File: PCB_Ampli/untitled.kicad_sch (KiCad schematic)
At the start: 58 parts

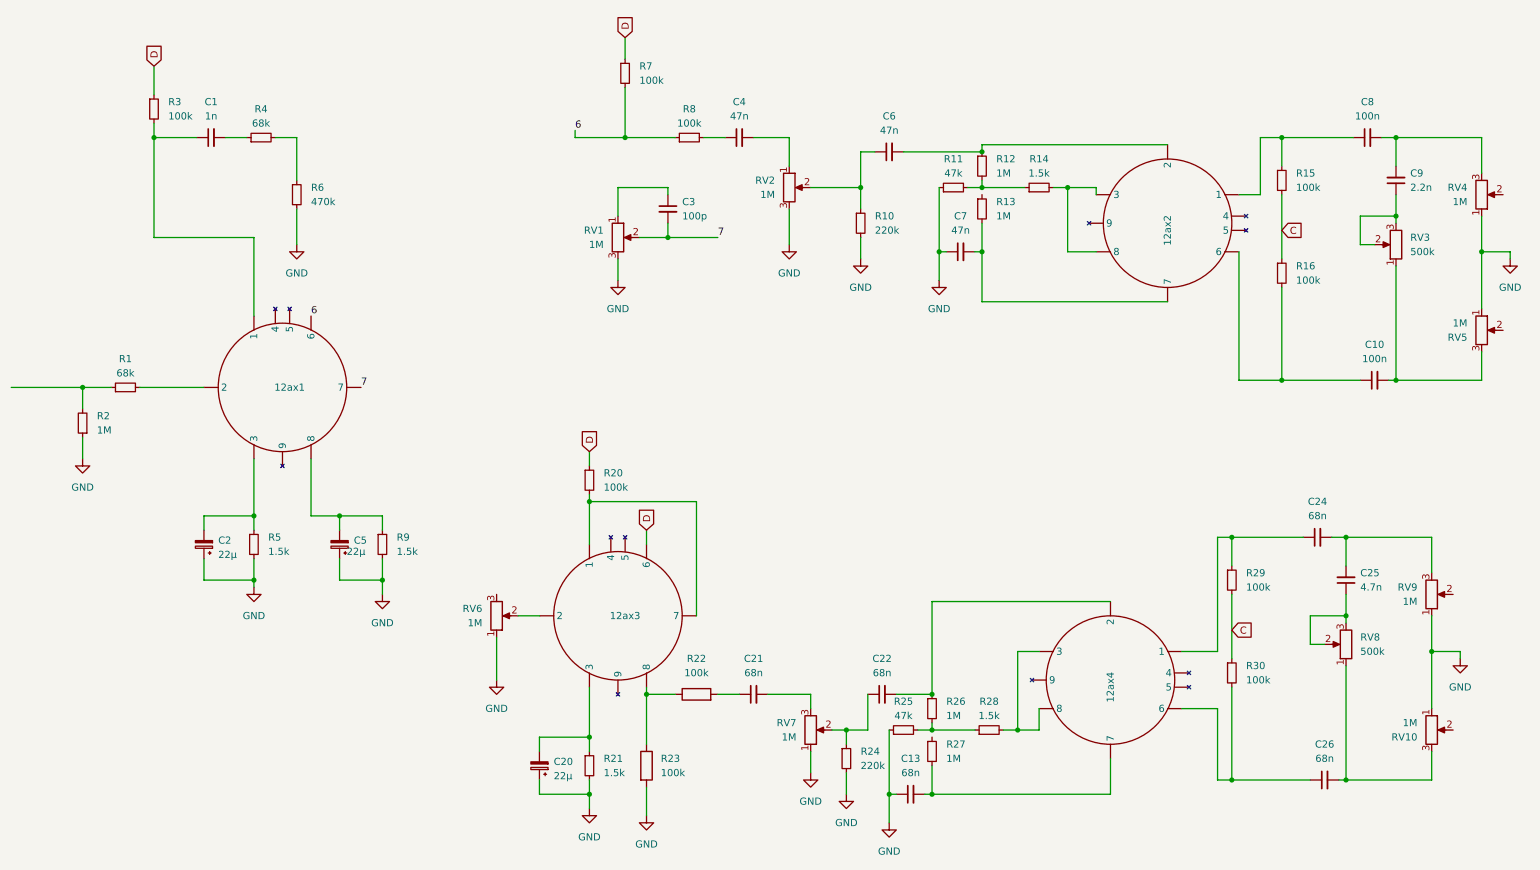
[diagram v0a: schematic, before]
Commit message: PCBV2_Part_Ampli_done
Amplification part using TPA3255 done
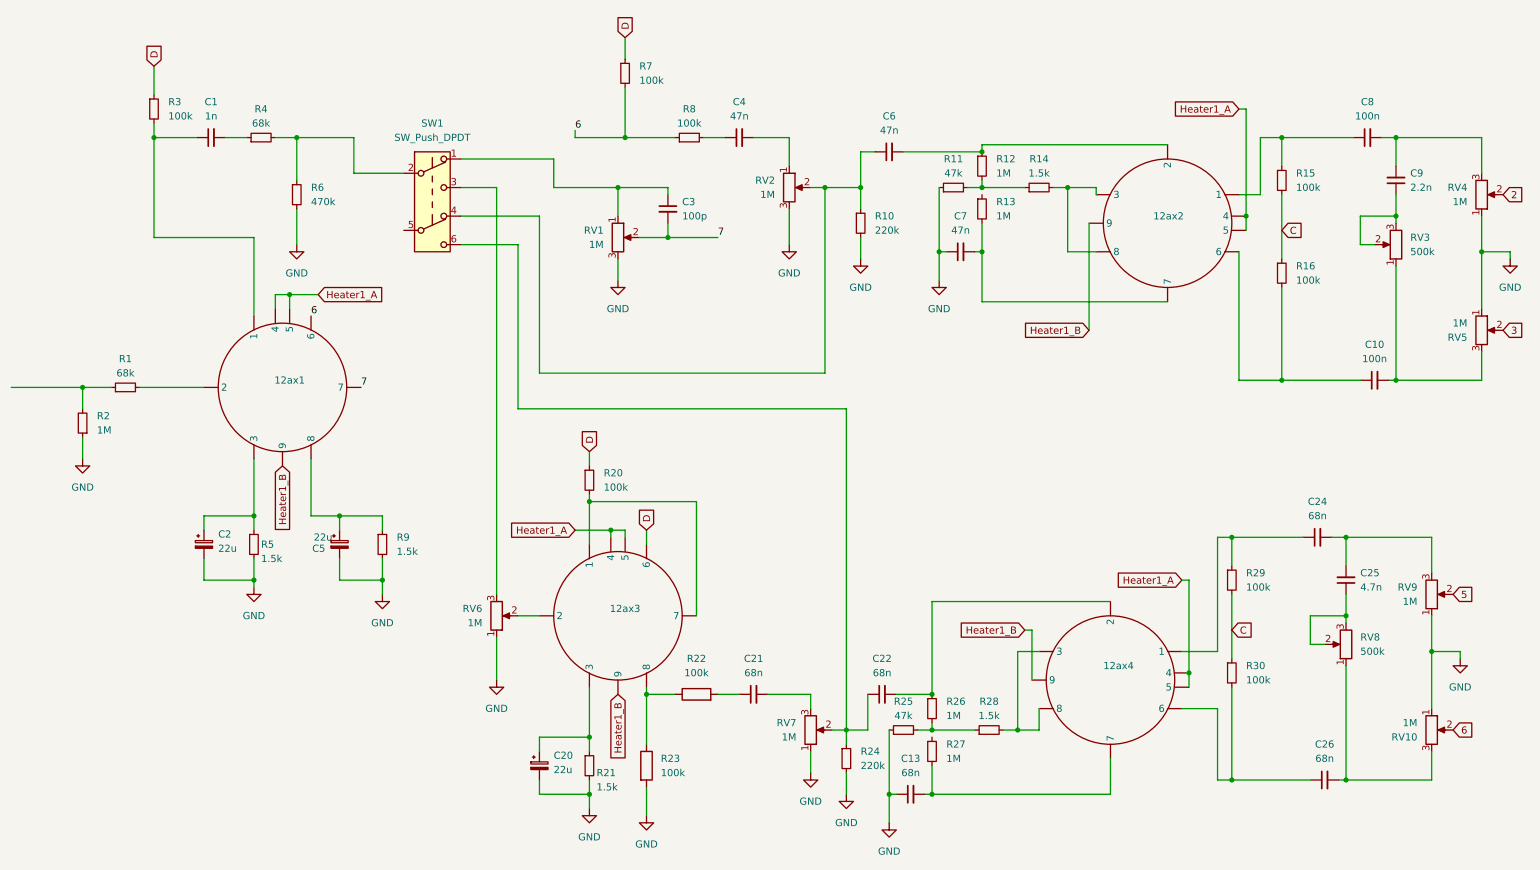
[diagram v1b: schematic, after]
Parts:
- added SW1: SW_Push_DPDT, symbol Switch:SW_Push_DPDT
- C2, C20, C5: value 22µ -> 22u
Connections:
- net 6: now also RV10.2
- net GND: now also C2.2, C20.2, C5.2; no longer C2.1, C20.1, C5.1
- net at C3.1, RV1.1: now also SW1.1 (A)
- net at C22.1, R24.1, RV7.2: now also SW1.6 (C)
- net 2: now reaches RV4.2
- net Heater1_B: now reaches 12ax2. (9)
- net Heater1_B: now also 12ax1. (9), 12ax3. (9), 12ax4. (9)
- net 5: now reaches RV9.2
- net at RV6.3: now also SW1.3 (C)
- net at R4.2, R6.1: now also SW1.2 (B)
- net at C6.1, R10.1, RV2.2: now also SW1.4 (A)
- net 3: now reaches RV5.2
- new net: 12ax3. (9), C20.1, R21.1
- new net: 12ax1. (9), C2.1, R5.1
- new net: 12ax1. (9), C5.1, R9.1
- new net Heater1_A: 12ax1. (9), 12ax2. (9), 12ax3. (9), 12ax4. (9)
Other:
- moved on the sheet: C2, C20, C5
